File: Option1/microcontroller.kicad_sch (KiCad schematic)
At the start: 15 parts, among them U801 ESP32-WROOM-32E-N4, U802 MCP23017_SO

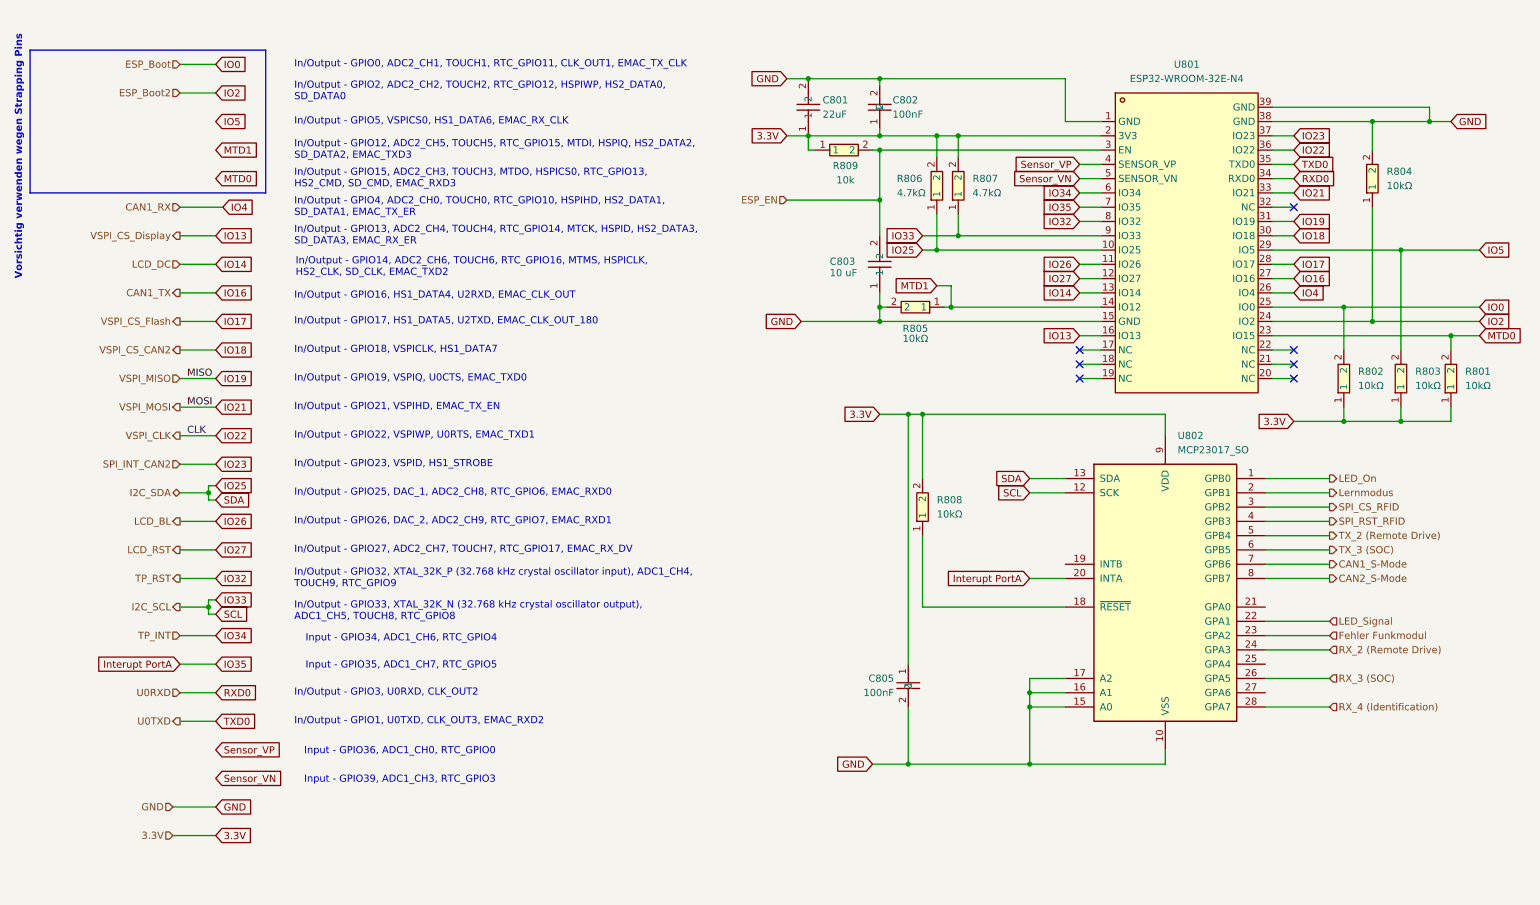
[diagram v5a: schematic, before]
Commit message: EasyEDA Lib in Projekt verschoben; Footprints, Silkscreen für designrule angepasst; Bauteilbeschriftungen entfernt, müssen neu angeordnet werden, JLC Rules eingebunden, Designrules erfolgreich bis auf Beschriftungen, Fehler in Radio Controll Beschaltung behoben; RFID Pinheader hinzugefügt
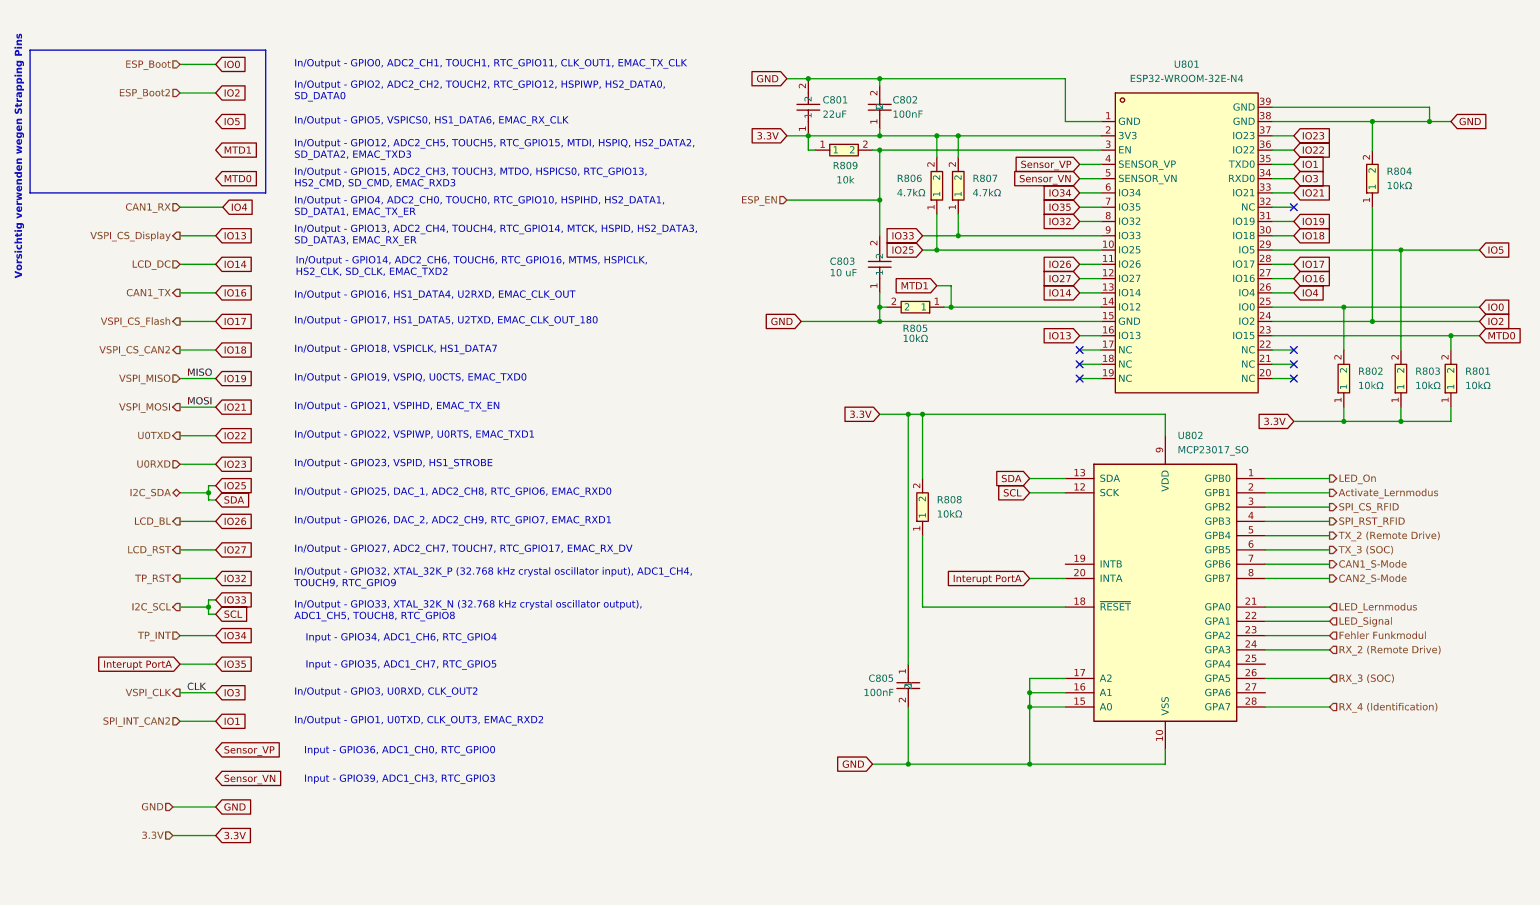
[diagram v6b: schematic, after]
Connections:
- net LED_Lernmodus: now reaches U802.21 (GPA0)
- net Lernmodus renamed Activate_Lernmodus
- net RXD0 renamed IO3
- net TXD0 renamed IO1
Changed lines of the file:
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@@
 	(wire
 		(pts
+			(xy 43.18 134.62) (xy 49.53 134.62)
+		)
+		(stroke
+			(width 0)
+			(type default)
+		)
+	)
+	(wire
+		(pts
 			(xy 181.61 48.26) (xy 207.01 48.26)
 		)
@@
 	(wire
 		(pts
+			(xy 236.22 93.98) (xy 247.65 93.98)
+		)
+		(stroke
+			(width 0)
+			(type default)
+		)
+	)
+	(wire
+		(pts
 			(xy 236.22 109.22) (xy 247.65 109.22)
 		)
@@
 	(wire
 		(pts
-			(xy 236.22 93.98) (xy 247.65 93.98)
-		)
-		(stroke
-			(width 0)
-			(type default)
-		)
-	)
-	(wire
-		(pts
 			(xy 194.31 109.22) (xy 200.66 109.22)
 		)
@@
 	(wire
 		(pts
+			(xy 236.22 114.3) (xy 247.65 114.3)
+		)
+		(stroke
+			(width 0)
+			(type default)
+		)
+	)
+	(wire
+		(pts
 			(xy 194.31 127) (xy 194.31 129.54)
 		)
@@
 	(wire
 		(pts
+			(xy 43.18 88.9) (xy 49.53 88.9)
+		)
+		(stroke
+			(width 0)
+			(type default)
+		)
+	)
+	(wire
+		(pts
 			(xy 203.2 45.72) (xy 207.01 45.72)
 		)
@@
 	(wire
 		(pts
-			(xy 43.18 88.9) (xy 49.53 88.9)
-		)
-		(stroke
-			(width 0)
-			(type default)
-		)
-	)
-	(wire
-		(pts
-			(xy 43.18 83.82) (xy 49.53 83.82)
+			(xy 43.18 129.54) (xy 49.53 129.54)
 		)
 		(stroke
@@
 	(wire
 		(pts
-			(xy 236.22 132.08) (xy 247.65 132.08)
+			(xy 43.18 83.82) (xy 49.53 83.82)
 		)
 		(stroke
@@
 	(wire
 		(pts
-			(xy 236.22 106.68) (xy 247.65 106.68)
+			(xy 236.22 132.08) (xy 247.65 132.08)
 		)
 		(stroke
@@
 	(wire
 		(pts
-			(xy 194.31 132.08) (xy 200.66 132.08)
+			(xy 236.22 106.68) (xy 247.65 106.68)
 		)
 		(stroke
@@
 	(wire
 		(pts
-			(xy 167.64 33.02) (xy 207.01 33.02)
+			(xy 194.31 132.08) (xy 200.66 132.08)
 		)
 		(stroke
@@
 	(wire
 		(pts
-			(xy 194.31 132.08) (xy 194.31 142.24)
+			(xy 167.64 33.02) (xy 207.01 33.02)
 		)
 		(stroke
@@
 	(wire
 		(pts
-			(xy 203.2 66.04) (xy 207.01 66.04)
+			(xy 194.31 132.08) (xy 194.31 142.24)
 		)
 		(stroke
@@
 	(wire
 		(pts
-			(xy 43.18 134.62) (xy 49.53 134.62)
+			(xy 203.2 66.04) (xy 207.01 66.04)
 		)
 		(stroke
@@
 	(wire
 		(pts
-			(xy 43.18 129.54) (xy 49.53 129.54)
-		)
-		(stroke
-			(width 0)
-			(type default)
-		)
-	)
-	(wire
-		(pts
 			(xy 237.49 38.1) (xy 241.3 38.1)
 		)
@@
 	)
 	(label "CLK"
-		(at 44.45 83.82 0)
+		(at 44.45 129.54 0)
 		(effects
 			(font
@@
 		)
 	)
-	(global_label "RXD0"
+	(global_label "IO3"
 		(shape input)
 		(at 49.53 129.54 0)
@@
 		)
 		(property "Intersheetrefs" "${INTERSHEET_REFS}"
-			(at 57.4742 129.54 0)
+			(at 55.66 129.54 0)
 			(effects
 				(font
@@
 		)
 	)
-	(global_label "TXD0"
+	(global_label "IO1"
 		(shape input)
 		(at 49.53 134.62 0)
@@
 		)
 		(property "Intersheetrefs" "${INTERSHEET_REFS}"
-			(at 57.1718 134.62 0)
+			(at 55.66 134.62 0)
 			(effects
 				(font
@@
 		)
 	)
-	(global_label "TXD0"
+	(global_label "IO1"
 		(shape input)
 		(at 241.3 35.56 0)
@@
 		)
 		(property "Intersheetrefs" "${INTERSHEET_REFS}"
-			(at 248.9418 35.56 0)
+			(at 247.43 35.56 0)
 			(effects
 				(font
@@
 		)
 	)
-	(global_label "RXD0"
+	(global_label "IO3"
 		(shape input)
 		(at 241.3 38.1 0)
@@
 		)
 		(property "Intersheetrefs" "${INTERSHEET_REFS}"
-			(at 249.2442 38.1 0)
+			(at 247.43 38.1 0)
 			(effects
 				(font
@@
 	(hierarchical_label "U0RXD"
 		(shape input)
-		(at 43.18 129.54 180)
+		(at 43.18 88.9 180)
 		(effects
 			(font
@@
 	(hierarchical_label "SPI_INT_CAN2"
 		(shape input)
-		(at 43.18 88.9 180)
+		(at 43.18 134.62 180)
 		(effects
 			(font
@@
 		)
 	)
-	(hierarchical_label "Lernmodus"
-		(shape output)
-		(at 247.65 93.98 0)
+	(hierarchical_label "LED_Lernmodus"
+		(shape input)
+		(at 247.65 114.3 0)
 		(effects
 			(font
@@
 	(hierarchical_label "U0TXD"
 		(shape output)
-		(at 43.18 134.62 180)
+		(at 43.18 83.82 180)
 		(effects
 			(font
@@
 		)
 	)
+	(hierarchical_label "Activate_Lernmodus"
+		(shape output)
+		(at 247.65 93.98 0)
+		(effects
+			(font
+				(size 1.27 1.27)
+			)
+			(justify left)
+		)
+	)
 	(hierarchical_label "VSPI_CLK"
 		(shape output)
-		(at 43.18 83.82 180)
+		(at 43.18 129.54 180)
 		(effects
 			(font

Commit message: Layout komplett neu überarbeitet, Neu Pinbelegung MCT, USB beschaltung muss noch korrigert werden
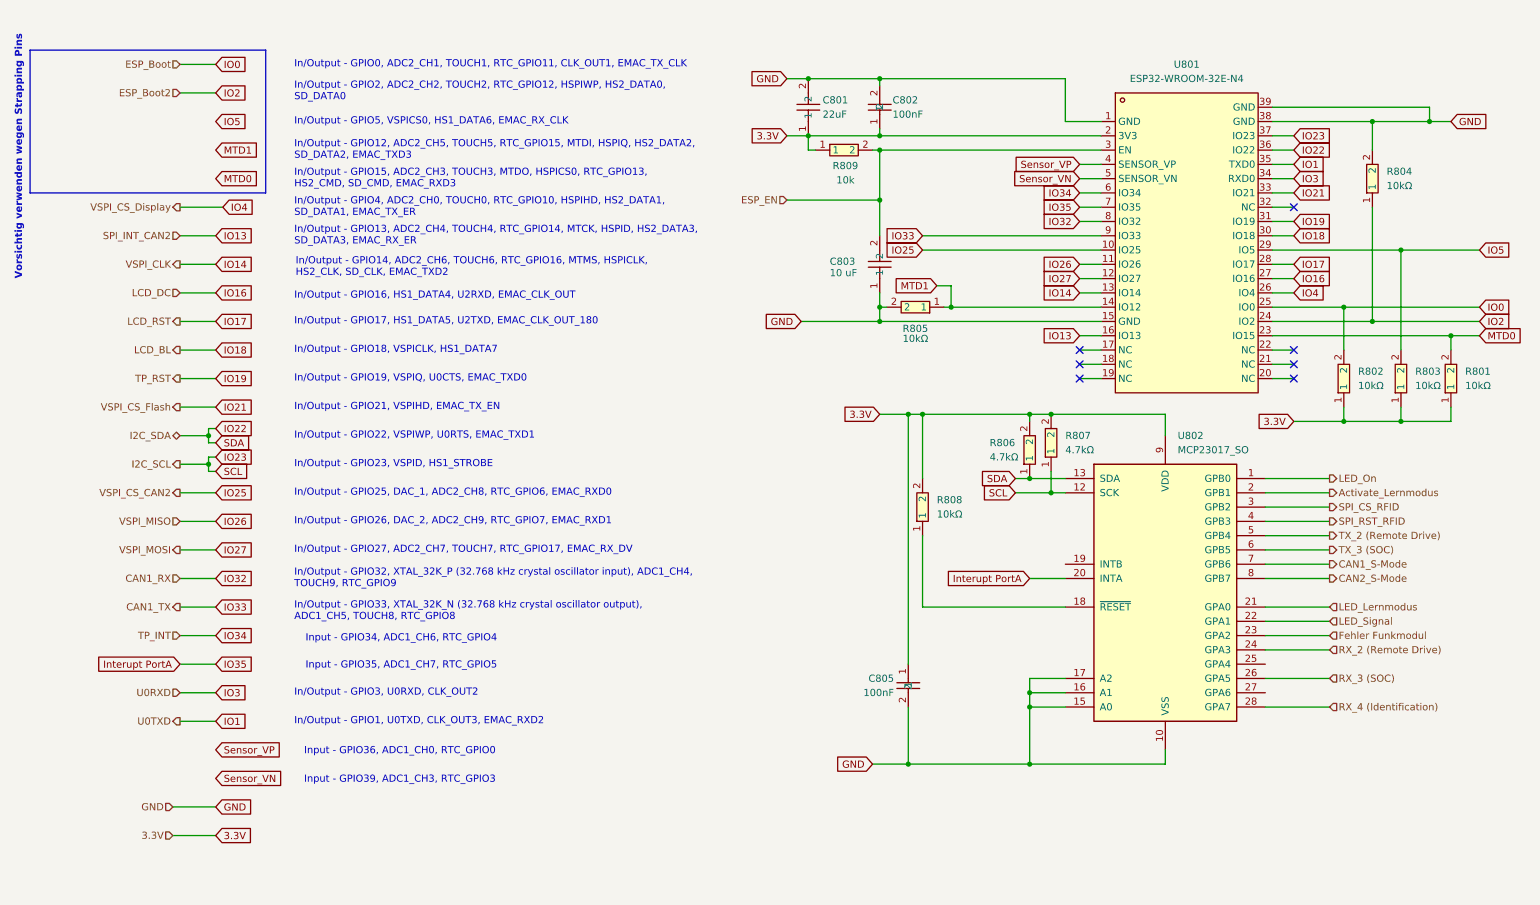
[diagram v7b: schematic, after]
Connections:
- net IO22: now also R806.1, U802.13 (SDA)
- net IO23: now also R807.1, U802.12 (SCK)
- net IO25: no longer R806.1, U802.13 (SDA)
- net IO33: no longer R807.1, U802.12 (SCK)
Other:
- moved on the sheet: R806, R807

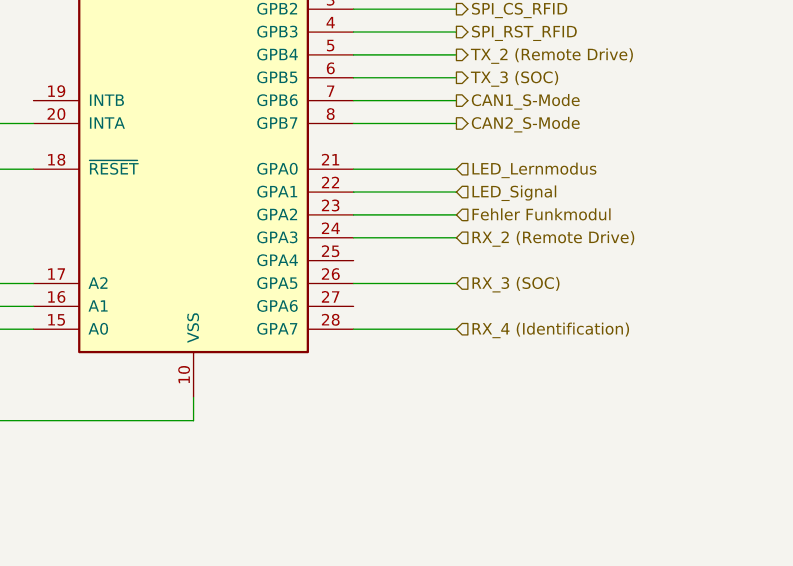
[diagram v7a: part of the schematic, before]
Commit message: power Supply angepasst für 12V und 48V, Datenblätter für DCDCs hinzugefügt
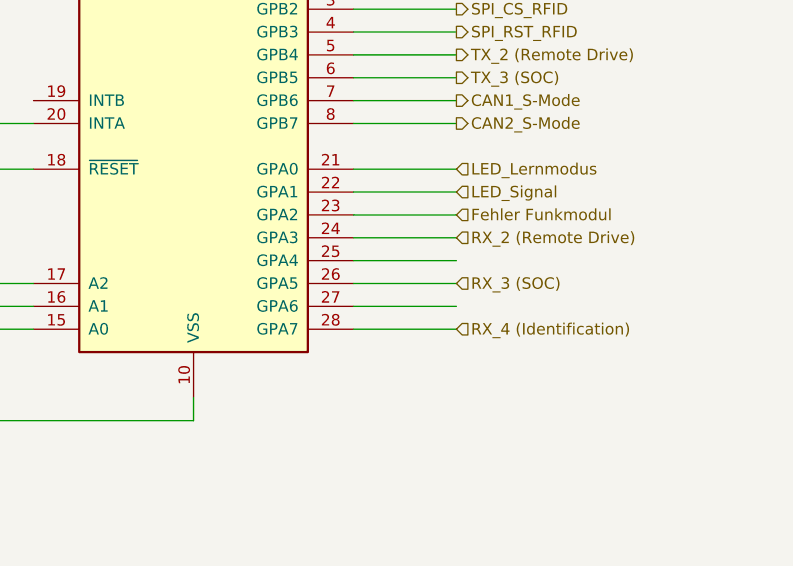
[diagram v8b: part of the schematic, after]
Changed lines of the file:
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@@
+	(wire
+		(pts
+			(xy 236.22 129.54) (xy 247.65 129.54)
+		)
+		(stroke
+			(width 0)
+			(type default)
+		)
+	)
 	(wire
 		(pts
@@
 		)
 		(stroke
+			(width 0)
+			(type default)
+		)
+	)
+	(wire
+		(pts
+			(xy 236.22 124.46) (xy 247.65 124.46)
+		)
+		(stroke
